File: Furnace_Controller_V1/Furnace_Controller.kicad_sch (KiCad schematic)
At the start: 34 parts, among them J1 Power In Treminal, J11 Conn_01x04_Socket, J2 Relay Terminal, J3 Relay Terminal, J4 HMD Terminal, J5 RS-485 Terminal, J6 Relay Terminal, J7 Relay Terminal, J8 Relay Terminal, J9 Relay Terminal, SW1 SW_Push, U1 ESP32-WROOM-32E-N8, U3 W25Q128JVS

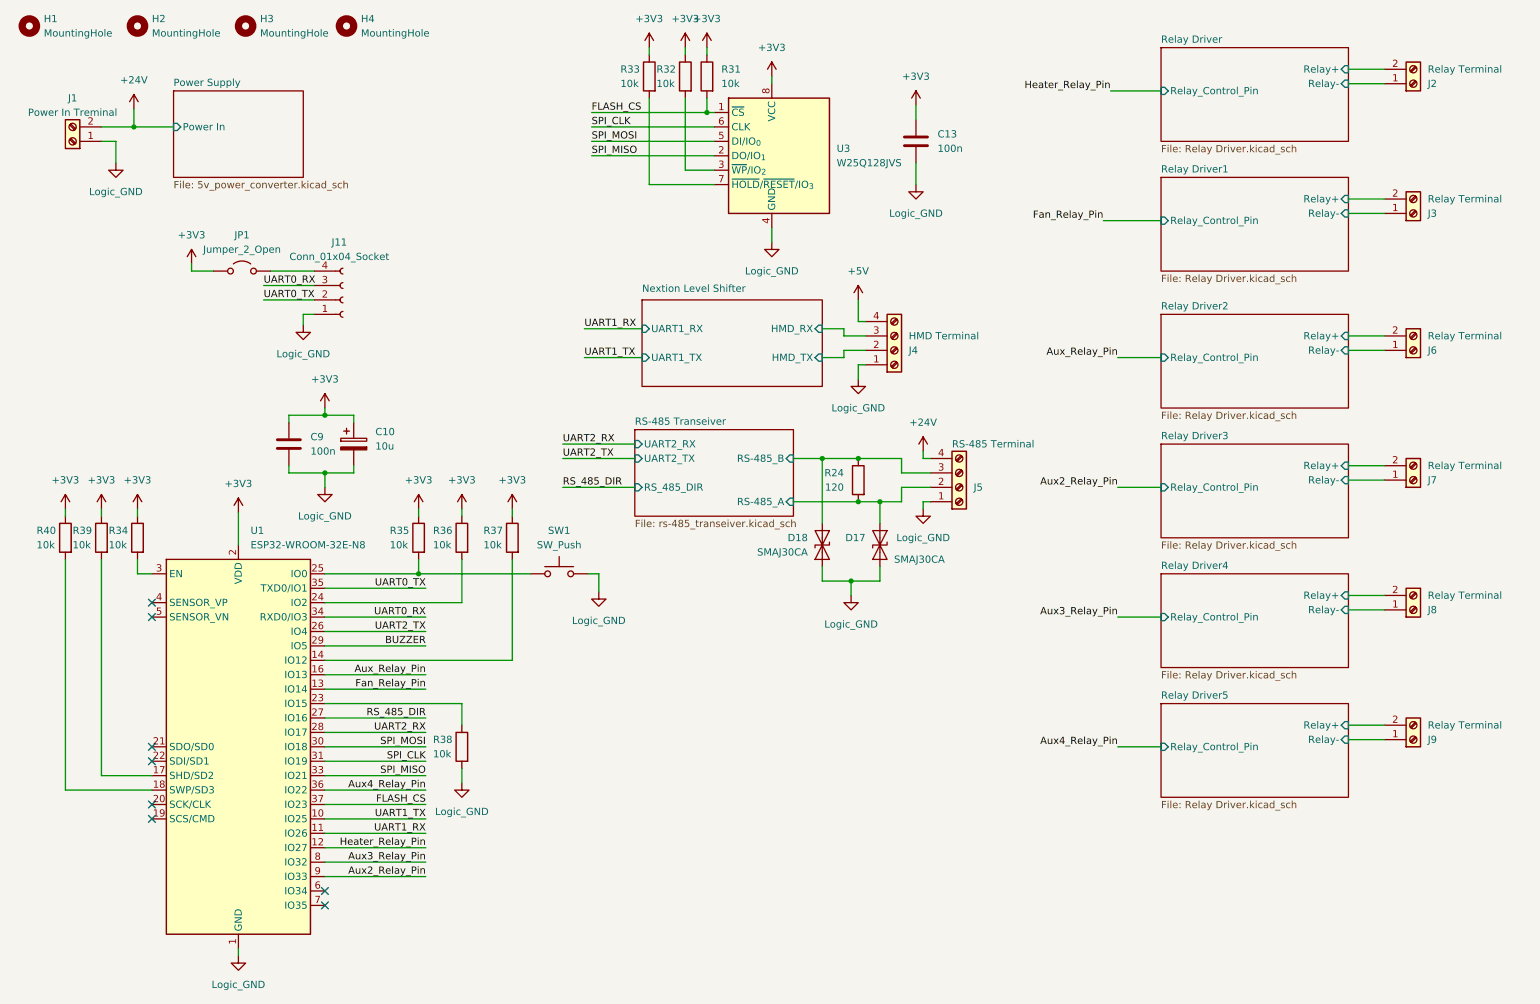
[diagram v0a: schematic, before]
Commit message: Organize PCB revisions and correct TI footprints
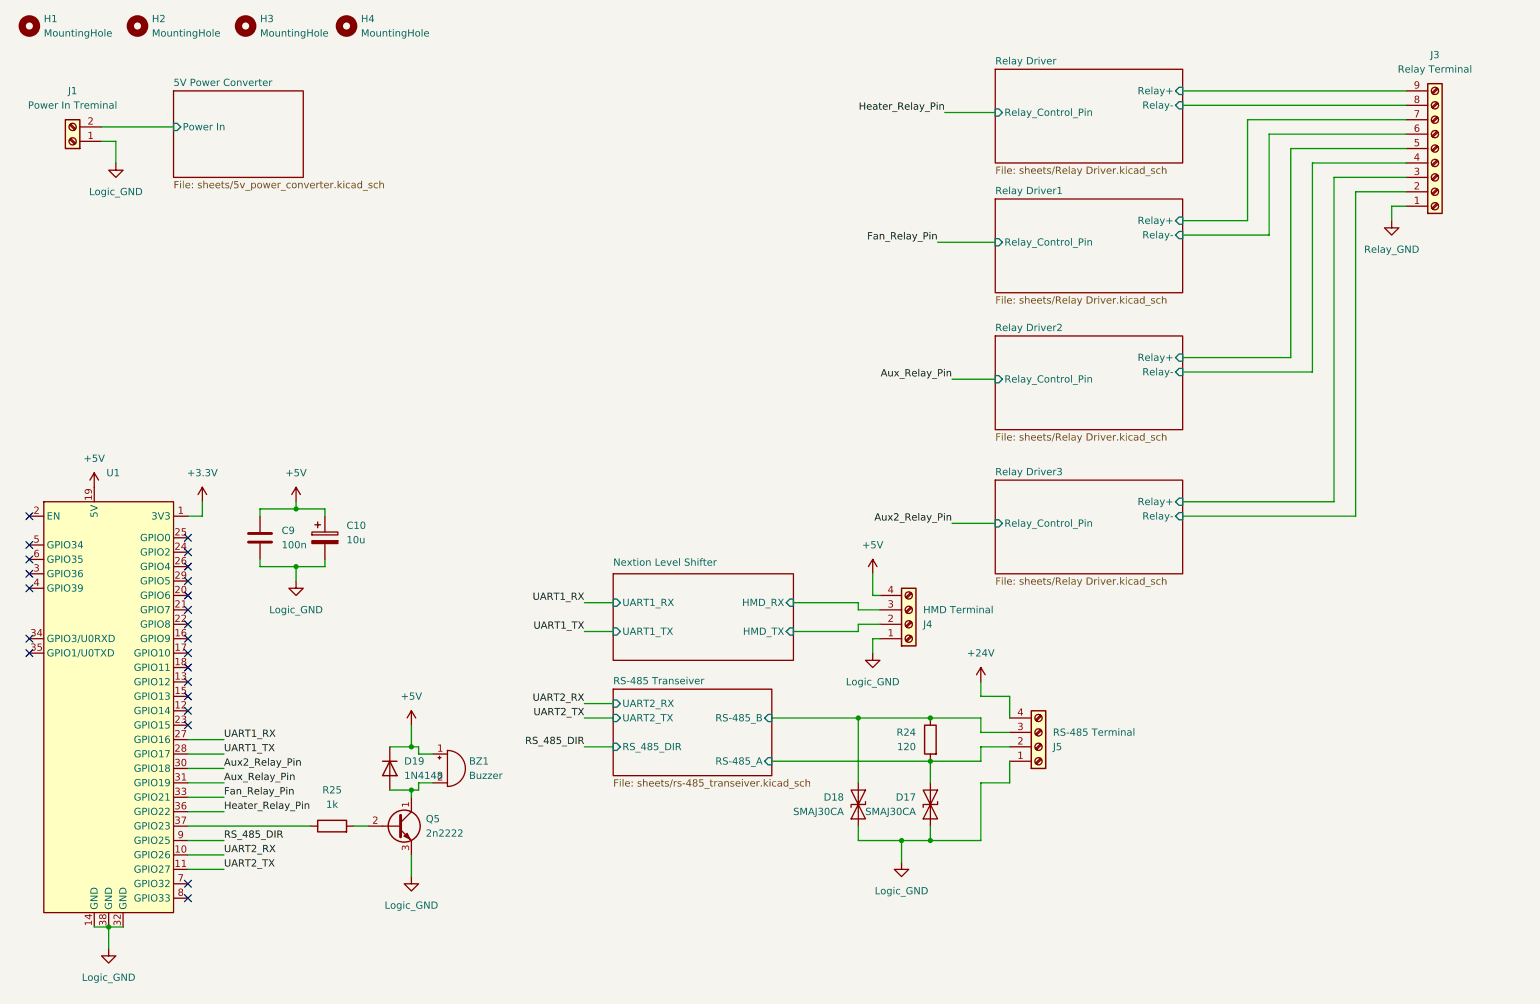
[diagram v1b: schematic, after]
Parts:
- removed C13: 100n, Capacitor_SMD:C_0603_1608Metric, symbol Device:C
- removed J11: Conn_01x04_Socket, Connector_PinHeader_2.54mm:PinHeader_1x04_P2.54mm_Vertical, symbol Connector:Conn_01x04_Socket
- removed J2, J3, J6, J7, J8, J9: Relay Terminal, Connector_Phoenix_MC:PhoenixContact_MC_1,5_2-G-3.5_1x02_P3.50mm_Horizontal, symbol Connector:Screw_Terminal_01x02
- removed JP1: Jumper_2_Open, TestPoint:TestPoint_2Pads_Pitch2.54mm_Drill0.8mm, symbol Jumper:Jumper_2_Open
- removed R31, R32, R33, R34, R35, R36, R37, R38, R39, R40: 10k, Resistor_SMD:R_0603_1608Metric, symbol Device:R
- removed SW1: SW_Push, Button_Switch_THT:SW_PUSH_6mm_H4.3mm, symbol Switch:SW_Push
- removed U1: ESP32-WROOM-32E-N8, RF_Module:ESP32-WROOM-32, symbol RF_Module:ESP32-WROOM-32
- removed U3: W25Q128JVS, Package_SO:SOIC-8_5.3x5.3mm_P1.27mm, symbol Memory_Flash:W25Q128JVS
- added BZ1: Buzzer, Buzzer_Beeper:Buzzer_15x7.5RM7.6, symbol Device:Buzzer
- added D19: 1N4148, Diode_THT:D_DO-35_SOD27_P7.62mm_Horizontal, symbol Diode:1N4148
- added J3: Relay Terminal, TerminalBlock:TerminalBlock_MaiXu_MX126-5.0-09P_1x09_P5.00mm, symbol Connector:Screw_Terminal_01x09
- added Q5: 2n2222, Package_TO_SOT_THT:TO-92_Inline, symbol Transistor_BJT:BC337
- added R25: 1k, Resistor_SMD:R_0805_2012Metric_Pad1.20x1.40mm_HandSolder, symbol Device:R
- added U1: ~, Custom_Footprints:ESP32_DevKitc_V4, symbol Custom_Symbols:ESP32_DevKitc_V4
- C9: footprint Capacitor_SMD:C_0603_1608Metric -> Capacitor_SMD:C_0805_2012Metric_Pad1.18x1.45mm_HandSolder
- J1: footprint Connector_Phoenix_MC:PhoenixContact_MC_1,5_2-G-3.5_1x02_P3.50mm_Horizontal -> TerminalBlock:TerminalBlock_MaiXu_MX126-5.0-02P_1x02_P5.00mm
- J4, J5: footprint Connector_Phoenix_MC:PhoenixContact_MC_1,5_4-G-3.5_1x04_P3.50mm_Horizontal -> TerminalBlock:TerminalBlock_MaiXu_MX126-5.0-04P_1x04_P5.00mm
- R24: footprint Resistor_SMD:R_0603_1608Metric -> Resistor_SMD:R_0805_2012Metric_Pad1.20x1.40mm_HandSolder
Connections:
- net +3V3 is gone; now on net +5V: C10.1, C9.1
- net +24V: no longer J1.2 (Pin_2)
- net +5V: now also BZ1.1 (+), D19.1 (K), U1.19 (5V)
- net Aux2_Relay_Pin: now also U1.30 (GPIO18)
- net Aux_Relay_Pin: now also U1.31 (GPIO19)
- net Fan_Relay_Pin: now also U1.33 (GPIO21)
- net Heater_Relay_Pin: now also U1.36 (GPIO22)
- net Logic_GND: now also Q5.3 (E), U1.14 (GND), U1.32 (GND), U1.38 (GND)
- net RS_485_DIR: now also U1.9 (GPIO25)
- net Relay Driver/Relay+: now also J3.9 (Pin_9)
- net Relay Driver/Relay-: now also J3.8 (Pin_8)
- net Relay Driver1/Relay+: now also J3.7 (Pin_7)
- net Relay Driver1/Relay-: now also J3.6 (Pin_6)
- net Relay Driver2/Relay+: now also J3.5 (Pin_5)
- net Relay Driver2/Relay-: now also J3.4 (Pin_4)
- net Relay Driver3/Relay+: now also J3.3 (Pin_3)
- net Relay Driver3/Relay-: now also J3.2 (Pin_2)
- net UART1_RX: now also U1.27 (GPIO16)
- net UART1_TX: now also U1.28 (GPIO17)
- net UART2_RX: now also U1.10 (GPIO26)
- net UART2_TX: now also U1.11 (GPIO27)
- new net: BZ1.2 (-), D19.2 (A), Q5.1 (C)
- new net: R25.1, U1.37 (GPIO23)
- new net: Q5.2 (B), R25.2
- new net +3.3V: U1.1 (3V3)
- new net 5V Power Converter/Power In: J1.2 (Pin_2)
- new net Relay_GND: J3.1 (Pin_1)
- no-connect marks 8 -> 23
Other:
- sheet Power Supply renamed 5V Power Converter
- removed sheet Relay Driver4
- removed sheet Relay Driver5
- sheet 5V Power Converter: file 5v_power_converter.kicad_sch -> sheets/5v_power_converter.kicad_sch
- sheet Nextion Level Shifter: file nextion_level_shifter.kicad_sch -> sheets/nextion_level_shifter.kicad_sch
- sheet RS-485 Transeiver: file rs-485_transeiver.kicad_sch -> sheets/rs-485_transeiver.kicad_sch
- sheet Relay Driver: file Relay Driver.kicad_sch -> sheets/Relay Driver.kicad_sch
- sheet Relay Driver1: file Relay Driver.kicad_sch -> sheets/Relay Driver.kicad_sch
- sheet Relay Driver2: file Relay Driver.kicad_sch -> sheets/Relay Driver.kicad_sch
- sheet Relay Driver3: file Relay Driver.kicad_sch -> sheets/Relay Driver.kicad_sch
- moved on the sheet: C10, C9, D17, D18, J4, J5, R24

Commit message: Normalize 3.3V net names
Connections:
- net +3.3V renamed +3V3
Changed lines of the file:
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@@
 	)
 	(symbol
-		(lib_id "power:+3.3V")
+		(lib_id "power:+3V3")
 		(at 48.26 99.06 0)
 		(unit 1)
@@
 			)
 		)
-		(property "Value" "+3.3V"
+		(property "Value" "+3V3"
 			(at 48.26 93.98 0)
 			(effects
@@
 			)
 		)
-		(property "Description" "Power symbol creates a global label with name \"+3.3V\""
+		(property "Description" "Power symbol creates a global label with name \"+3V3\""
 			(at 48.26 99.06 0)
 			(effects
